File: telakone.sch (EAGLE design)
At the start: 27 parts, among them X2 MPT0.5/8-2.54

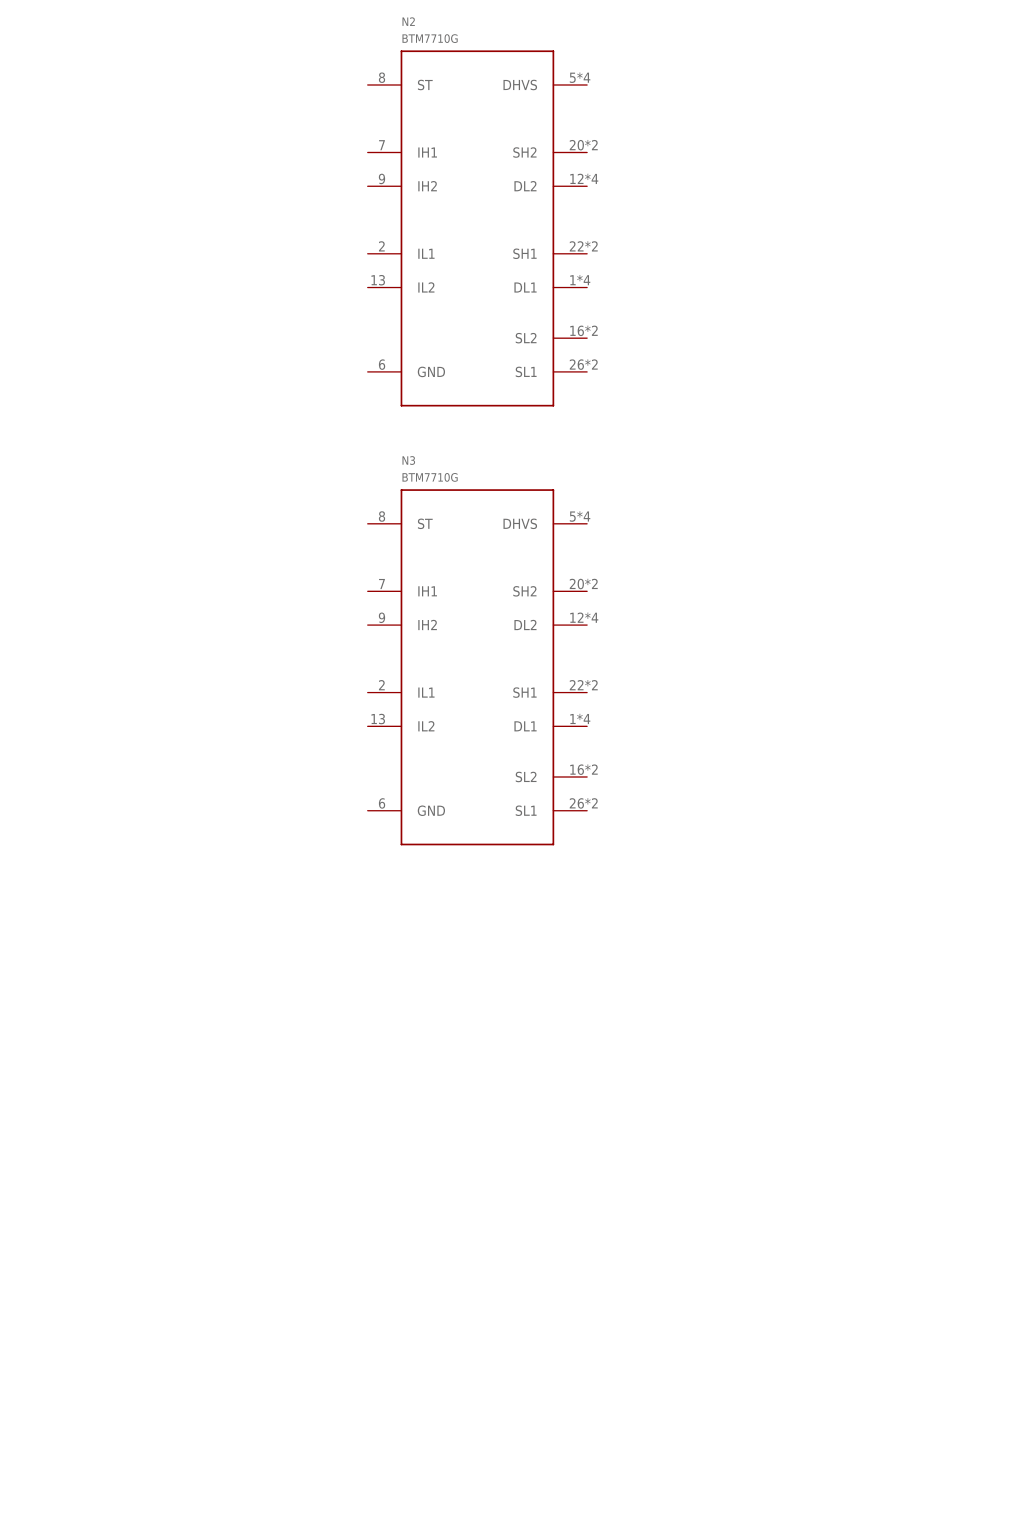
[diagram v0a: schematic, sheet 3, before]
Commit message: p-fet outputs
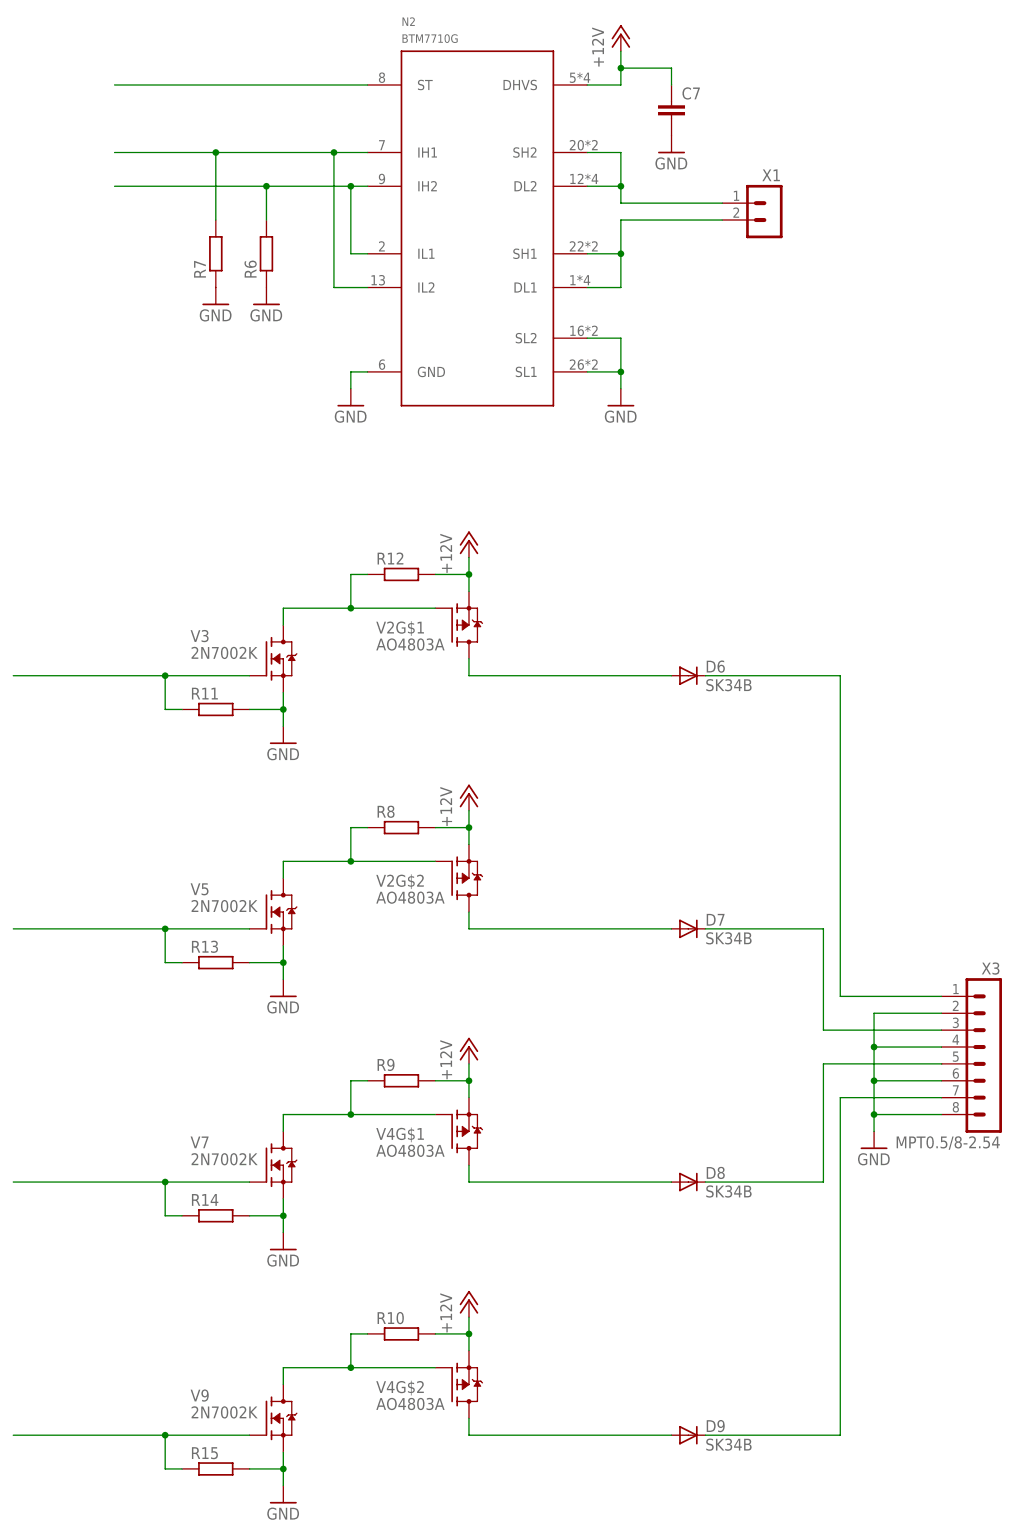
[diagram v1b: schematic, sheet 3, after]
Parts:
- removed N3: BTM7710G, omat_ic_2:BTM7710G
- added C7: (no value), omat_ic_2:CAP0805
- added D6, D7, D8, D9: SK34B, diode:DIODE-SMB
- added R10, R11, R12, R13, R14, R15, R6, R7, R8, R9: (no value), omat_ic_2:RES0603
- added V2, V4: AO4803A, omat_ic_2:AO4803A
- added V3, V5, V7, V9: 2N7002K, omat_ic_2:2N7002K
- added X1: (no value), omat_ic_2:TE_RUUVILIITIN2
- added X3: MPT0.5/8-2.54, omat_ic_2:MPT0.5/8-2.54
- D2: value STPS340U -> SK34B
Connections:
- new net +12V: C2.1, C3.1, C7.1, N1.VIN, N2.DHVS, R10.2, R12.2, R8.2, R9.2, V2G$1.S, V2G$2.S, V4G$1.S, V4G$2.S
- new net N$10: R8.1, V2G$2.G, V5.D
- new net N$11: R12.1, V2G$1.G, V3.D
- new net N$12: R13.1, V5.G
- new net N$13: R9.1, V4G$1.G, V7.D
- new net N$14: R14.1, V7.G
- new net N$15: R10.1, V4G$2.G, V9.D
- new net N$16: R15.1, V9.G
- new net N$17: D9.C, X3.7
- new net N$19: D8.C, X3.5
- new net N$20: D7.C, X3.3
- new net N$21: D6.C, X3.1
- new net N$3: N2.DL2, N2.SH2, X1.1
- new net N$5: N2.DL1, N2.SH1, X1.2
- new net N$7: N2.ST
- new net N$8: N2.IH1, N2.IL2, R7.2
- new net N$9: N2.IH2, N2.IL1, R6.2
- new net NERT: D6.A, V2G$1.D
- new net NERT1: D7.A, V2G$2.D
- new net NERT2: D8.A, V4G$1.D
- new net NERT3: D9.A, V4G$2.D
- net GND: now also C7.2, N2.GND, N2.SL1, N2.SL2, R11.2, R13.2, R14.2, R15.2, R6.1, R7.1, V3.S, V5.S, V7.S, V9.S, X3.2, X3.4, X3.6, X3.8
- net N$6: now also R11.1, V3.G; no longer C2.1, C3.1, N1.VIN

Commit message: placement sketching, temp and acceleration sensors, 2nd drive group
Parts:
- removed D2, D6, D7, D8, D9: SK34B, diode:DIODE-SMB
- removed D3, D4: 1SMA5.0AT, EKE:1SMA5913BT3
- added C10, C11, C12, C13, C14, C15, C16, C17, C18, C19, C20, C21, C22, C23, C24, C26, C27, C28, C29, C30, C31, C32, C33, C34, C35, C36, C38, C39, C40, C41, C42, C43, C44, C8, C9: (no value), omat_ic_2:CAP0603
- added C25: 10p, omat_ic_2:CAP0603
- added C37, C45: (no value), EKE:CPOL-EUCT7343
- added D10: RT9818C-29GV, omat_ic_2:RT9818C-29GV
- added D11: LM75BD, omat_ic_2:LM75BD
- added D12: IIS328DQTR, omat_ic_2:IIS328DQTR
- added D15: SI8661-IS1, omat_ic_2:SI8661-IS1
- added G1: 25MHz, omat_ic_2:XTAL_3225_SMD
- added L2: IND0603, omat_ic_2:IND0603
- added N10: MCP3201/SN, omat_ic_2:MCP3201/SN
- added N11, N3: MCP1501/SN, omat_ic_2:MCP1501/SN
- added N8: MCP4921/SN, omat_ic_2:MCP4921/SN
- added N9: TS921IDT, omat_ic_2:TS921IDT
- added R16, R17, R18, R19, R20, R21, R22, R23, R27, R28, R29, R32: (no value), omat_ic_2:RES0603
- added R24, R25: 22, omat_ic_2:RES0603
- added R26: 1k, omat_ic_2:RES0603
- added R30: 825, omat_ic_2:RES0603
- added R31: 19k1, omat_ic_2:RES1206
- added V10, V11, V12, V13, V8: SK34B, diode:DIODE-SMB
- added V14, V15, V16, V17: 1SMA5.0AT, EKE:1SMA5913BT3
- added V6: AO4886, omat_ic_2:AO4886
- added X4: PIIKKIRIMA-2, omat_ic_2:PIIKKIRIMA-2
- added X5: PIIKKIRIMA-5, omat_ic_2:PIIKKIRIMA-5
- added X6: (no value), omat_ic_2:TE_RUUVILIITIN2
- added X7: U.FL-R-SMT-1, omat_ic_2:U.FL-R-SMT-1
- added X8: MPT0.5/8-2.54, omat_ic_2:MPT0.5/8-2.54
- added X9: 629105136821, omat_ic_2:629105136821
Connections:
- net +48V renamed +48V_1
- net BRAKE renamed BRAKE_1
- net BRAKE_OD renamed BRAKE_OD_1
- net REVERSE renamed REVERSE_1
- net REVERSE_OD renamed REVERSE_OD_1
- net SPICLK renamed SPICLK_1
- net SPICSL renamed SPICSL_1
- net SPIMISO renamed SPIMISO_1
- net SPIMOSI renamed SPIMOSI_1
- net THROTTLE renamed THROTTLE_1
- net THROTTLE_BUFFERED renamed THROTTLE_BUFFERED_1
- net VREF+2V5 renamed VREF25_1
- removed net AIN: C5.1, D4.C, N6.IN+, R3.2, R4.2
- removed net V+: D3.C, D5.VCC2, N4.VDD, N5.V+, N6.VDD, N7.SHDNL, N7.VDD, X2.4
- removed net V-: C5.2, C6.2, D3.A, D4.A, D5.GND2, N4.LDACL, N4.VSSA, N5.V-, N6.IN-, N6.VSS, N7.GND@1, N7.GND@2, N7.GND@3, N7.GND@4, R3.1, V1G$1.S, V1G$2.S, X2.3, X2.8
- new net +48V_2: R31.1, X8.1, X8.2
- new net AIN_1: C5.1, N6.IN+, R3.2, R4.2, V14.C
- new net AIN_2: C38.1, N10.IN+, R30.2, R31.2, V16.C
- new net BOOT0: D1G$1.BOOT0, R19.2, X4.2
- new net BRAKE_2: D15.OUT4, V6G$1.G
- new net BRAKE_OD_2: V6G$1.D, X8.6
- new net CCHIBL: A1.HIBL, D1G$2.PA2
- new net CCIRQ: A1.IRQ, D1G$2.PA4
- new net CCSPICLK: A1.SPI_CLK, D1G$2.PA5
- new net CCSPICSL: A1.SPI_CSL, D1G$2.PA3
- new net CCSPIMISO: A1.SPI_DOUT, D1G$2.PA6
- new net CCSPIMOSI: A1.SPI_DIN, D1G$2.PA7
- new net I2CSCL: D11.SCL, D12.SCL/SPICLK, D1G$2.PB6, R29.1
- new net I2CSDA: D11.SDA, D12.SDA/SPISDI, D1G$2.PB7, R28.1
- new net N$22: C8.1, D1G$1.VCAP2
- new net N$23: C9.1, D1G$1.VCAP1
- new net N$24: C12.1, R17.1
- new net N$25: C10.1, C11.1, D1G$1.VDDA, L2.1
- new net N$26: C23.1, D1G$1.PH0/OSCIN, G1.X1
- new net N$27: D1G$1.PH1/OSCOUT, R18.2
- new net N$28: C24.1, G1.X2, R18.1
- new net N$29: D1G$1.PB2/BOOT1, R20.2
- new net N$30: A1.RF_BG, C25.1
- new net N$31: C25.2, X7.2
- new net N$32: A1.RSVD, R21.2
- new net N$33: D1G$2.PA11, R24.2
- new net N$34: A1.FORCEAP, R22.2
- new net N$35: A1.TCXO_EN/SOP2, R23.2
- new net N$36: D1G$2.PA12, R25.2
- new net N$37: R25.1, X9.3
- new net N$38: R24.1, X9.2
- new net N$39: D1G$2.PA9, R26.2
- new net N$40: R26.1, X9.1
- new net N$41: D1G$2.PA10, R27.2
- new net N$42: C39.1, R32.1
- new net RESETL: A1.RESETL, D10.RESET, D1G$1.RSTL, R16.1, X5.4
- new net REVERSE_2: D15.OUT5, V6G$2.G
- new net REVERSE_OD_2: V6G$2.D, X8.7
- new net SPICLK_2: D15.OUT2, N10.SCK, N8.SCK
- new net SPICSL_2: D15.OUT1, N10.CSL, N8.CSL
- new net SPIMISO_2: D15.IN6, N10.SDO
- new net SPIMOSI_2: D15.OUT3, N8.SDI
- new net SWCLK: D1G$1.PA14/TCK/SWCLK, X5.3
- new net SWDIO: D1G$1.PA13/TMS/SWDIO, X5.2
- new net THROTTLE_2: N8.VOUTA, N9.+IN
- new net THROTTLE_BUFFERED_2: N9.-IN, N9.OUT, X8.5
- new net V+1: C32.1, C33.1, C34.1, C35.1, C36.1, C37.+, D5.VCC2, N4.VDD, N5.V+, N6.VDD, N7.SHDNL, N7.VDD, V15.C, X2.4
- new net V+2: C40.1, C41.1, C42.1, C43.1, C44.1, C45.+, D15.VCC2, N10.VDD, N11.SHDNL, N11.VDD, N8.VDD, N9.V+, V17.C, X8.4
- new net V-1: C32.2, C33.2, C34.2, C35.2, C36.2, C37.-, C5.2, C6.2, D5.GND2, N4.LDACL, N4.VSSA, N5.V-, N6.IN-, N6.VSS, N7.GND@1, N7.GND@2, N7.GND@3, N7.GND@4, R3.1, V14.A, V15.A, V1G$1.S, V1G$2.S, X2.3, X2.8
- new net V-2: C38.2, C39.2, C40.2, C41.2, C42.2, C43.2, C44.2, C45.-, D15.GND2, N10.IN-, N10.VSS, N11.GND@1, N11.GND@2, N11.GND@3, N11.GND@4, N8.LDACL, N8.VSSA, N9.V-, R30.1, V16.A, V17.A, V6G$1.S, V6G$2.S, X8.3, X8.8
- new net VREF25: D1G$1.VREF+, N3.FEEDBACK, N3.OUT, R17.2
- new net VREF25_2: N10.VREFA, N11.FEEDBACK, N11.OUT, N8.VREFA, R32.2
- net +12V: now also X6.1
- net +3V3: now also A1.VBAT_ANA, A1.VBAT_DIGIO, A1.VBAT_PA, C13.1, C14.1, C15.1, C16.1, C17.1, C18.1, C19.1, C20.1, C21.1, C22.1, C26.1, C27.1, C28.1, C29.1, C30.1, C31.1, D10.VCC, D11.VCC, D12.CS, D12.RSVD1, D12.VDD, D12.VDDIO, D15.VCC1, D1G$1.PDR_ON, D1G$1.VBAT, D1G$1.VDD1, D1G$1.VDD10, D1G$1.VDD11, D1G$1.VDD12, D1G$1.VDD2, D1G$1.VDD3, D1G$1.VDD4, D1G$1.VDD5, D1G$1.VDD6, D1G$1.VDD7, D1G$1.VDD8, D1G$1.VDD9, L2.2, N3.SHDNL, N3.VDD, R16.2, R27.1, R28.2, R29.2, X4.1, X5.1
- net GND: now also A1.GND@1, A1.GND@10, A1.GND@11, A1.GND@12, A1.GND@13, A1.GND@14, A1.GND@15, A1.GND@16, A1.GND@17, A1.GND@18, A1.GND@2, A1.GND@3, A1.GND@4, A1.GND@5, A1.GND@6, A1.GND@7, A1.GND@8, A1.GND@9, C10.2, C11.2, C12.2, C13.2, C14.2, C15.2, C16.2, C17.2, C18.2, C19.2, C20.2, C21.2, C22.2, C23.2, C24.2, C26.2, C27.2, C28.2, C29.2, C30.2, C31.2, C8.2, C9.2, D10.GND, D11.A0, D11.A1, D11.A2, D11.GND, D12.EP, D12.GND@1, D12.GND@2, D12.GND@3, D12.GND@4, D12.RSVD2, D12.SAO/SPISDO, D15.GND1, D1G$1.VSS1, D1G$1.VSS2, D1G$1.VSS3, D1G$1.VSS4, D1G$1.VSS5, D1G$1.VSS6, D1G$1.VSS7, D1G$1.VSS8, D1G$1.VSS9, D1G$1.VSSA, N3.GND@1, N3.GND@2, N3.GND@3, N3.GND@4, R19.1, R20.1, R21.1, R22.1, R23.1, V13.A, X5.5, X6.2, X7.1, X7.3, X9.5; no longer D2.A
- net N$1: now also V13.C; no longer D2.C
- net N$17: now also V12.C; no longer D9.C
- net N$19: now also V11.C; no longer D8.C
- net N$20: now also V10.C; no longer D7.C
- net N$21: now also V8.C; no longer D6.C
- net NERT: now also V8.A; no longer D6.A
- net NERT1: now also V10.A; no longer D7.A
- net NERT2: now also V11.A; no longer D8.A
- net NERT3: now also V12.A; no longer D9.A
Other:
- note added: "2.5V REFERENCE"
- note added: "BOOTMODE"
- note added: "I2C ADDR: 0011000 (18H)"
- note added: "I2C ADDR: 1001000 (48H)"
- note added: "SPI1"
- note added: "SW DEBUG"

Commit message: joystick inputs, change motor driver to plain fets, motor current measurement
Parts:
- removed C7: (no value), omat_ic_2:CAP0805
- added C47, C48, C49: (no value), omat_ic_2:CAP0603
- added N12: TS921IDT, omat_ic_2:TS921IDT
- added R33, R34, R37, R38, R43, R44, R45, R46: (no value), omat_ic_2:RES0603
- added R35: 5k90, omat_ic_2:RES1206
- added R36: 825, omat_ic_2:RES0603
- added R39: ERJ-8BWFR010V, omat_ic_2:RES1206
- added R40: 10, omat_ic_2:RES0603
- added R41: 499, omat_ic_2:RES0603
- added V18, V20: 2N7002K, omat_ic_2:2N7002K
- added V19: AO4803A, omat_ic_2:AO4803A
- added V22: AO4886, omat_ic_2:AO4886
- added X11: MPT0.5/8-2.54, omat_ic_2:MPT0.5/8-2.54
- N2: value BTM7710G -> LTC2050CS8; device omat_ic_2:BTM7710G -> omat_ic_2:LTC2050CS8
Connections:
- net I2CSCL renamed I2C1SCL
- net I2CSDA renamed I2C1SDA
- net N$22 renamed VCAP2
- net N$23 renamed VCAP1
- net N$25 renamed VDDA
- removed net N$16: R15.1, V9.G
- removed net N$8: N2.IH1, N2.IL2, R7.2
- new net BUTTON1: D1G$3.PF1, R45.1, X11.1
- new net BUTTON2: D1G$3.PF2, R46.1, X11.2
- new net D1BRAKE: D1G$2.PB10, D5.IN4
- new net D1REVERSE: D1G$2.PB11, D5.IN5
- new net D1SPICLK: D1G$2.PB13, D5.IN2
- new net D1SPICSL: D1G$2.PB12, D5.IN1
- new net D1SPIMISO: D1G$2.PB14, D5.OUT6
- new net D1SPIMOSI: D1G$2.PB15, D5.IN3
- new net D2BRAKE: D15.IN4, D1G$2.PC7
- new net D2REVERSE: D15.IN5, D1G$2.PC8
- new net D2SPICLK: D1G$2.PC10
- new net D2SPICSL: D15.IN1, D1G$2.PC9
- new net D2SPIMISO: D15.OUT6, D1G$2.PC11
- new net D2SPIMOSI: D15.IN3, D1G$2.PC12
- new net DSPICLK: D15.IN2
- new net MEAS12V: C47.1, D1G$1.PA0/WKUP, R35.2, R36.2
- new net MOTOR_CURR: D1G$3.PF3, N2.OUT, R41.1
- new net MOTOR_H1: D1G$3.PE5, R7.1, V18.G
- new net MOTOR_H2: D1G$3.PE6, R34.1, V20.G
- new net MOTOR_L1: D1G$3.PE3, R37.1, V22G$1.G
- new net MOTOR_L2: D1G$3.PE4, R38.1, V22G$2.G
- new net NERT4: V19G$2.D, V22G$1.D, X1.1
- new net NERT5: V19G$1.D, V22G$2.D, X1.2
- new net OUT1: D1G$3.PF6, R11.1, V3.G
- new net OUT2: D1G$3.PF7, R13.1, V5.G
- new net OUT3: D1G$3.PF8, R14.1, V7.G
- new net OUT4: D1G$3.PF9, R15.1, V9.G
- new net POT1: C49.1, D1G$3.PF4, R43.1
- new net POT2: C48.1, D1G$3.PF5, R44.1
- net +12V: now also R33.2, R35.1, R6.2, V19G$1.S, V19G$2.S; no longer C7.1, N2.DHVS
- net +3V3: now also N12.V+, N2.SD, N2.V+, R45.2, R46.2
- net GND: now also C47.2, C48.2, C49.2, N12.V-, N2.V-, R34.2, R36.1, R39.1, R40.2, R7.2, V18.S, V20.S, X11.5, X11.8; no longer C7.2, N2.GND, N2.SL1, N2.SL2, R6.1, R7.1
- net N$12: now also R43.2, X11.4; no longer R13.1, V5.G
- net N$14: now also R44.2, X11.7; no longer R14.1, V7.G
- net N$3: now also R6.1, V18.D, V19G$2.G; no longer N2.DL2, N2.SH2, X1.1
- net N$5: now also N12.-IN, N12.OUT, X11.3, X11.6; no longer N2.DL1, N2.SH1, X1.2
- net N$6: now also R33.1, V19G$1.G, V20.D; no longer R11.1, V3.G
- net N$7: now also N2.+IN, R37.2, R38.2, R39.2, V22G$1.S, V22G$2.S; no longer N2.ST
- net N$9: now also N2.-IN, R40.1, R41.2; no longer N2.IH2, N2.IL1, R6.2
- net VREF25: now also N12.+IN
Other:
- note added: "ADC3_IN9 ADC3_IN14 ADC3_IN15 TIM10_CH1 TIM11_CH1 TIM13_CH1 TIM14_CH1"
- note added: "I2C1"
- note added: "JOYSTICK"
- note added: "MAX 20V ~4.97mV/LSB ADC123_in0"
- note added: "SPI2"
- note added: "SPI3"
- note added: "TIM9_CH1 TIM9_CH2"
- note added: "~0.61mV/LSB"
- note added: "~1.2mA/LSB"
